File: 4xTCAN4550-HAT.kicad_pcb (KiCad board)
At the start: 4 copper layers, 27.2 x 55 mm, 67 parts, among them J1 Conn_02x04_Odd_Even, J2 Raspberry_Pi_2_3, U1 LM27313XMF, U2 AT24CS64-MAHM, U3 TCAN4550, U4 TCAN4550, U5 TCAN4550, U6 TCAN4550, X1 ASV-40.000MHz

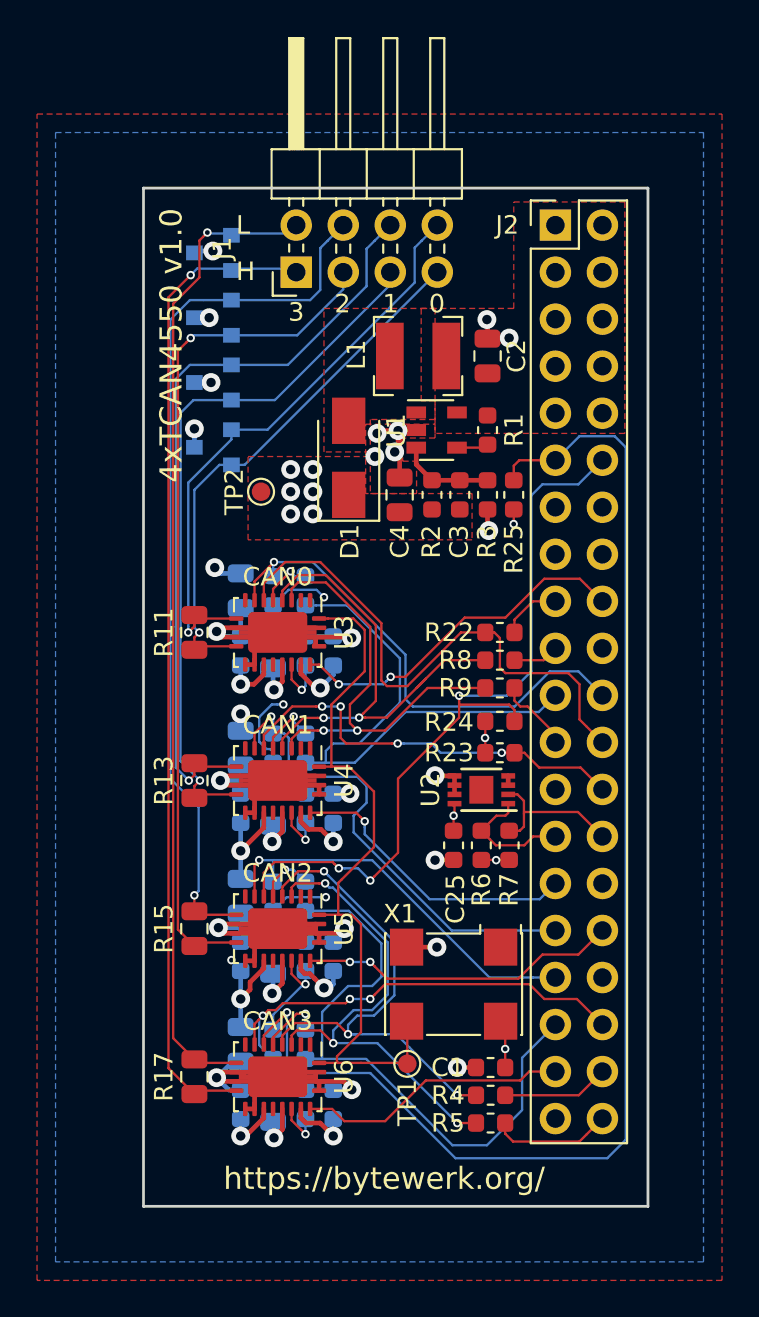
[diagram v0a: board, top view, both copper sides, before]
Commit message: fix eeprom
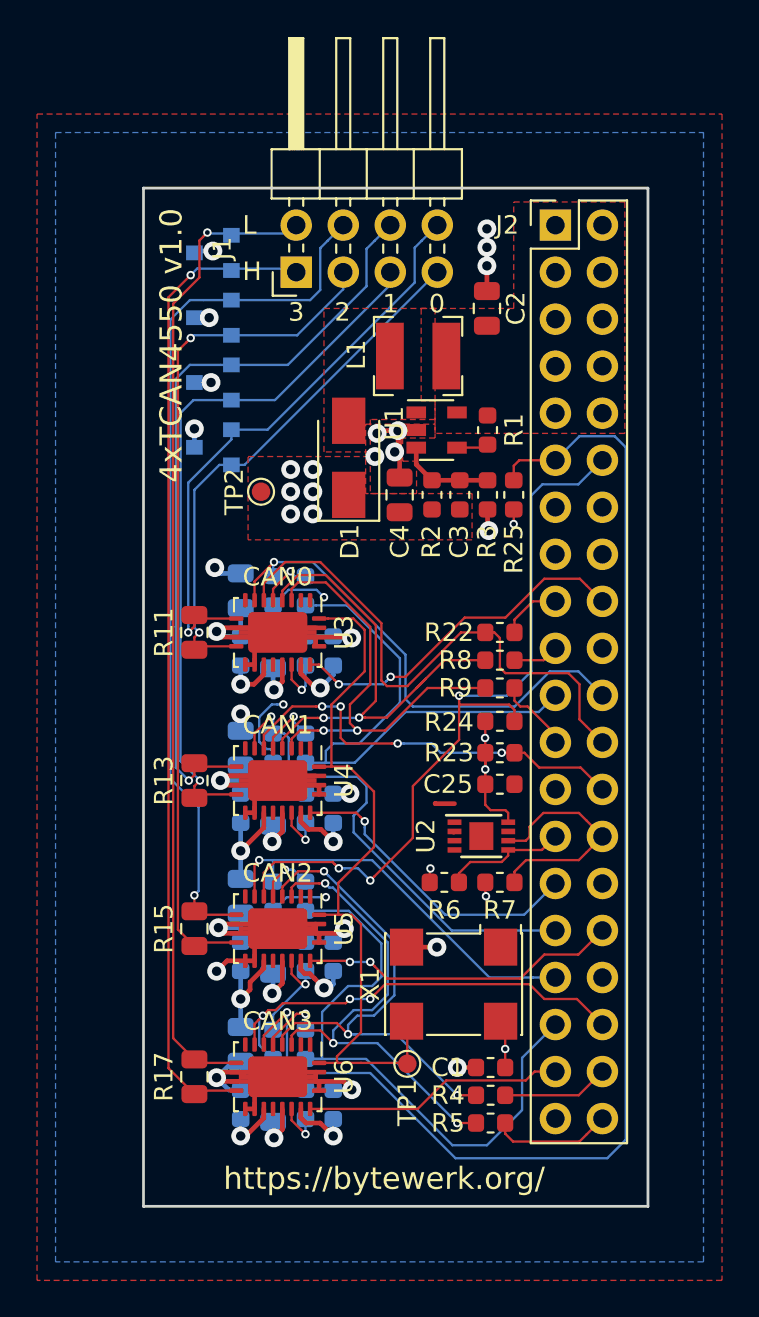
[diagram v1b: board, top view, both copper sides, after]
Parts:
- moved C25 4.14 mm to (155.0, 102.2), turned to 0 degrees
- moved R6 2.83 mm to (152.0, 107.5), turned to 0 degrees
- moved C2 2.57 mm to (154.3, 76.5)
- moved U2 2.50 mm to (154.0, 105.0), turned to 0 degrees
- moved R7 2.06 mm to (155.0, 107.5), turned to 0 degrees
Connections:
- U2 pad 1: Net-(J2-Pad27) -> GND
- U2 pad 2: Net-(J2-Pad28) -> GND
- U2 pad 5: GND -> Net-(J2-Pad27)
- U2 pad 6: GND -> Net-(J2-Pad28)
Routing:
- net Net-(J2-Pad28): track 8.06 -> 12.7 mm
- net +3V3: track 36.7 -> 40.6 mm, vias 12 -> 13
- net /Raspi HAT/CAN1_RST: track 15.9 -> 16.6 mm
- net /Raspi HAT/CAN3_RST: track 14.6 -> 14.1 mm
- net GND: track 104.5 -> 105.0 mm, vias 24 -> 23

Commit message: remove rst, add wake and is_awake
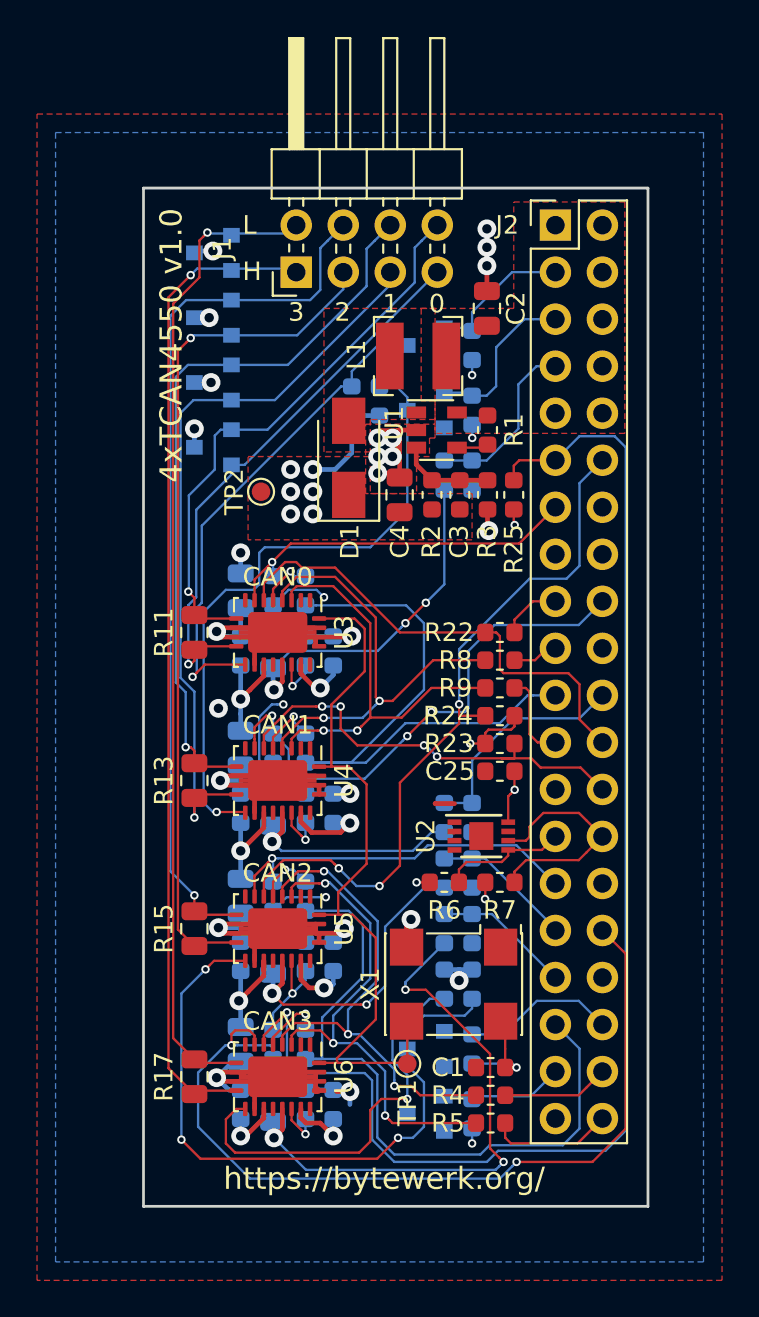
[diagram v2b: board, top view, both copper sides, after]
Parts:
- added Q1: 2N7002, Package_TO_SOT_SMD:SOT-23, B.Cu at (151.0, 78.5)
- added Q2: 2N7002, Package_TO_SOT_SMD:SOT-23, B.Cu at (151.0, 82.0)
- added Q3: 2N7002, Package_TO_SOT_SMD:SOT-23, B.Cu at (151.0, 116.5)
- added Q4: 2N7002, Package_TO_SOT_SMD:SOT-23, B.Cu at (151.0, 120.0)
- added R26: 10K, Resistor_SMD:R_0603_1608Metric, B.Cu at (153.5, 78.5)
- added R27: 10K, Resistor_SMD:R_0603_1608Metric, B.Cu at (147.0, 81.5)
- added R28: 5K6, Resistor_SMD:R_0603_1608Metric, B.Cu at (152.0, 85.5)
- added R29: 10K, Resistor_SMD:R_0603_1608Metric, B.Cu at (153.5, 85.5)
- added R30: 10K, Resistor_SMD:R_0603_1608Metric, B.Cu at (153.5, 82.0)
- added R31: 10K, Resistor_SMD:R_0603_1608Metric, B.Cu at (148.5, 81.5)
- added R32: 5K6, Resistor_SMD:R_0603_1608Metric, B.Cu at (152.0, 104.0)
- added R33: 10K, Resistor_SMD:R_0603_1608Metric, B.Cu at (153.5, 104.0)
- added R34: 10K, Resistor_SMD:R_0603_1608Metric, B.Cu at (153.5, 116.5)
- added R35: 10K, Resistor_SMD:R_0603_1608Metric, B.Cu at (153.5, 113.0)
- added R36: 5K6, Resistor_SMD:R_0603_1608Metric, B.Cu at (152.0, 107.0)
- added R37: 10K, Resistor_SMD:R_0603_1608Metric, B.Cu at (153.5, 107.0)
- added R38: 10K, Resistor_SMD:R_0603_1608Metric, B.Cu at (153.5, 120.0)
- added R39: 10K, Resistor_SMD:R_0603_1608Metric, B.Cu at (152.0, 113.0)
- added R40: 5K6, Resistor_SMD:R_0603_1608Metric, B.Cu at (152.0, 110.0)
- added R41: 10K, Resistor_SMD:R_0603_1608Metric, B.Cu at (153.5, 110.0)
- moved C25 0.70 mm to (155.0, 101.5), turned to 180 degrees
- moved R23 0.50 mm to (155.0, 100.0)
- moved R24 0.30 mm to (155.0, 98.5), turned to 180 degrees
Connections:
- J2 pad 13: Net-(J2-Pad13) -> /Raspi HAT/CAN0_INT
- J2 pad 18: /Raspi HAT/CAN0_RST -> /Raspi HAT/CAN1_INT
- J2 pad 22: /Raspi HAT/CAN0_INT -> /Raspi HAT/CAN1_IS_AWAKE
- J2 pad 29: /Raspi HAT/CAN1_RST -> /Raspi HAT/CAN2_INT
- J2 pad 3: Net-(J2-Pad3) -> /Raspi HAT/CAN0_WAKE
- J2 pad 31: /Raspi HAT/CAN1_INT -> /Raspi HAT/CAN2_IS_AWAKE
- J2 pad 32: /Raspi HAT/CAN2_RST -> /Raspi HAT/CAN3_INT
- J2 pad 33: /Raspi HAT/CAN2_INT -> /Raspi HAT/CAN3_IS_AWAKE
- J2 pad 36: /Raspi HAT/CAN3_INT -> /Raspi HAT/CAN2_WAKE
- J2 pad 37: /Raspi HAT/CAN3_RST -> /Raspi HAT/CAN3_WAKE
- J2 pad 5: Net-(J2-Pad5) -> /Raspi HAT/CAN1_WAKE
- J2 pad 7: Net-(J2-Pad7) -> /Raspi HAT/CAN0_IS_AWAKE
- U3 pad 12: GND -> Net-(Q1-Pad3)
- U3 pad 19: /Raspi HAT/CAN0_RST -> /CAN0/RST
- U4 pad 12: GND -> Net-(Q2-Pad3)
- U4 pad 19: /Raspi HAT/CAN1_RST -> /CAN1/RST
- U5 pad 12: GND -> Net-(Q3-Pad3)
- U5 pad 19: /Raspi HAT/CAN2_RST -> /CAN2/RST
- U6 pad 12: GND -> Net-(Q4-Pad3)
- U6 pad 19: /Raspi HAT/CAN3_RST -> /CAN3/RST
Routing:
- net Net-(Q3-Pad3): track 0.00 -> 36.3 mm, vias 0 -> 3
- net Net-(Q2-Pad3): track 0.00 -> 34.9 mm, vias 0 -> 1
- net Net-(C20-Pad1): track 2.63 -> 31.4 mm, vias 1 -> 3
- net Net-(Q1-Pad3): track 0.00 -> 27.1 mm, vias 0 -> 1
- net Net-(Q4-Pad3): track 0.00 -> 23.1 mm, vias 0 -> 1
- net /Raspi HAT/CAN3_INT: track 24.4 -> 47.4 mm, vias 3 -> 2
- net VCC: track 19.7 -> 42.1 mm
- net /Raspi HAT/CAN0_RST: track 19.1 -> 0.00 mm, vias 2 -> 0
- net /Raspi HAT/CAN2_RST: track 17.3 -> 0.00 mm, vias 2 -> 0
- net /Raspi HAT/CAN1_RST: track 16.6 -> 0.00 mm, vias 1 -> 0
- net Net-(C5-Pad1): track 2.73 -> 19.0 mm, vias 1 -> 3
- net /Raspi HAT/CAN3_RST: track 14.1 -> 0.00 mm
- net Net-(C15-Pad1): track 3.07 -> 17.1 mm, vias 1 -> 2
- net /Raspi HAT/CAN1_IS_AWAKE: track 0.00 -> 12.3 mm
- net Net-(C10-Pad1): track 2.67 -> 12.6 mm
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
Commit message: move wake fet pull-ups from transceivers to raspi-hat schematic page
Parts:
- C12, C17, C22, C7: value 330nF -> 1uF
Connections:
- net /CAN0/RST renamed Net-(U3-Pad19)
- net /CAN1/RST renamed Net-(U4-Pad19)
- net /CAN2/RST renamed Net-(U5-Pad19)
- net /CAN3/RST renamed Net-(U6-Pad19)
